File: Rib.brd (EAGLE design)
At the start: 127 x 87.6 mm, 34 parts, among them IC1 REG1117, IC2 REG1117

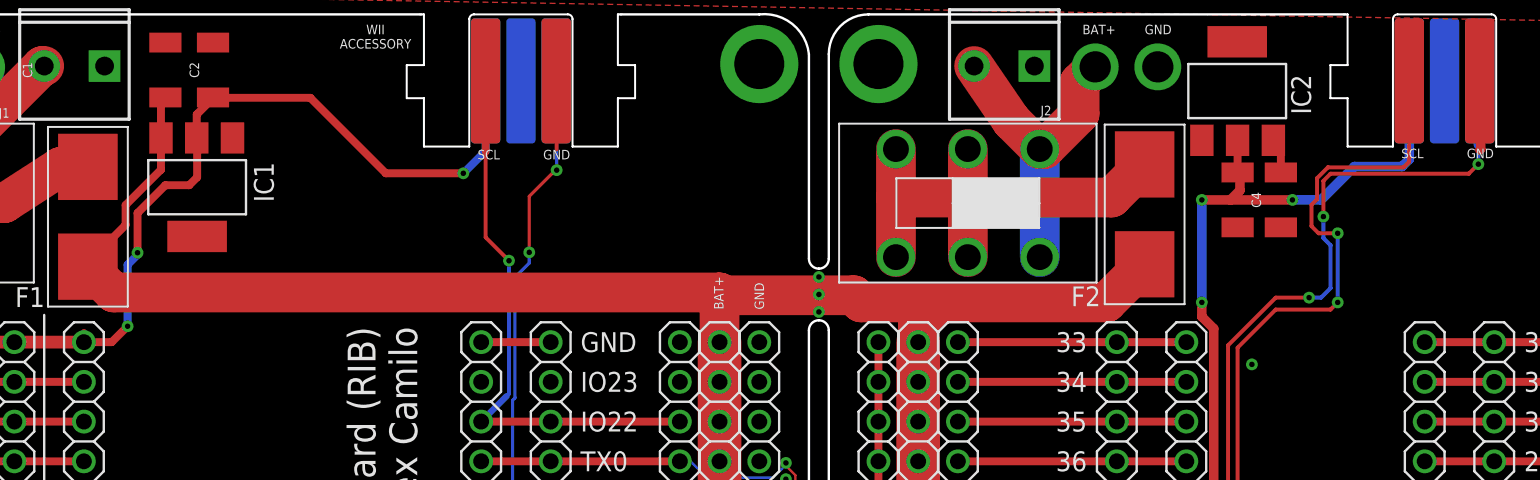
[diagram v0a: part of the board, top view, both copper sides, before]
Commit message: DET pins routed to esp and teensy
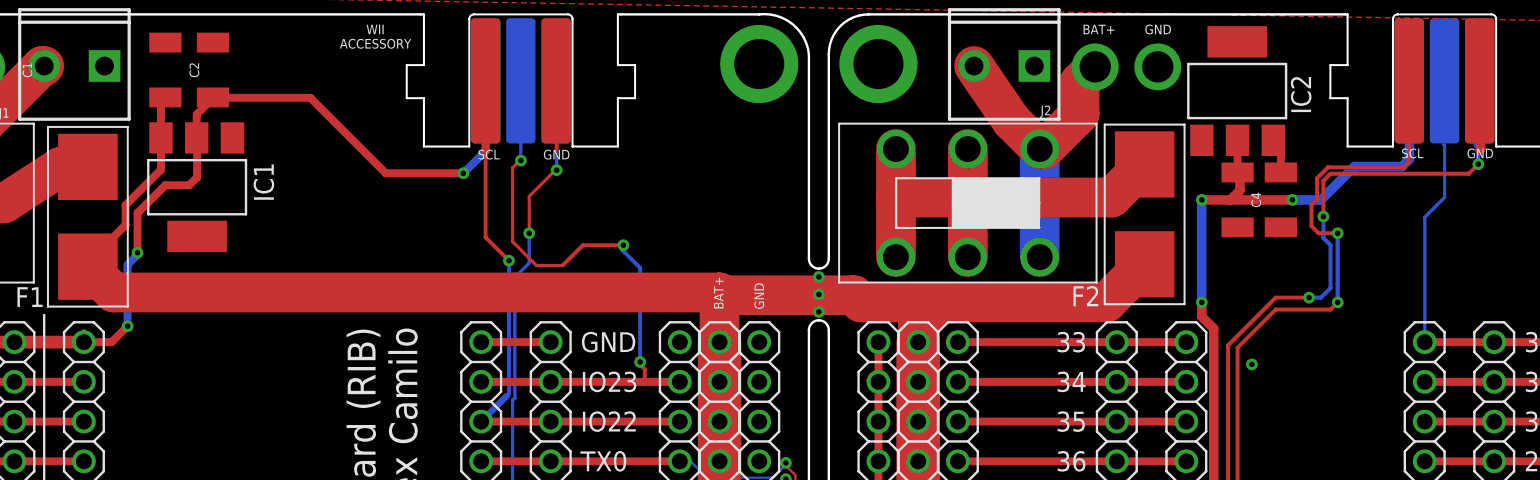
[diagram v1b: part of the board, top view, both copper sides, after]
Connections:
- removed net N$107: JP12.24, JP21.24, JP9.24
- removed net N$24: JP17.18, JP7.18, JP8.18
- new net DET: JP12.24, JP17.18, JP21.24, JP7.18, JP8.18, JP9.24, U$3.ATT, U$5.ATT
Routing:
- net DET: track 0.00 -> 62.5 mm, vias 0 -> 3
- net N$107: track 12.1 -> 0.00 mm
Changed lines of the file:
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@@
 <via x="49.53" y="53.848" extent="1-16" drill="0.35"/>
 <via x="49.53" y="52.7304" extent="1-16" drill="0.35"/>
-<wire x1="4.445" y1="53.975" x2="43.18" y2="53.975" width="2.54" layer="1"/>
+<wire x1="4.445" y1="53.975" x2="30.099" y2="53.975" width="2.54" layer="1"/>
+<wire x1="30.099" y1="53.975" x2="43.18" y2="53.975" width="2.54" layer="1"/>
 <wire x1="67.9196" y1="53.34" x2="70.358" y2="55.7784" width="2.54" layer="1"/>
 <wire x1="67.9196" y1="53.34" x2="57.15" y2="53.34" width="2.54" layer="1"/>
@@
 <via x="29.9466" y="39.243" extent="1-16" drill="0.35"/>
 <wire x1="29.9466" y1="39.243" x2="29.9466" y2="47.08001875" width="0.2032" layer="16"/>
-<wire x1="30.099" y1="54.9402" x2="31.0134" y2="55.8546" width="0.2032" layer="16"/>
 <wire x1="29.9466" y1="47.08001875" x2="30.099" y2="47.23241875" width="0.2032" layer="16"/>
 <wire x1="30.099" y1="47.23241875" x2="30.099" y2="54.9402" width="0.2032" layer="16"/>
-<via x="31.0134" y="56.5404" extent="1-16" drill="0.35"/>
-<wire x1="31.0134" y1="56.5404" x2="31.0134" y2="60.1218" width="0.2032" layer="1"/>
+<via x="31.0134" y="57.7596" extent="1-16" drill="0.35"/>
+<wire x1="31.0134" y1="57.7596" x2="31.0134" y2="60.1218" width="0.2032" layer="1"/>
 <wire x1="31.0134" y1="60.1218" x2="32.6136" y2="61.722" width="0.2032" layer="1"/>
 <wire x1="32.6136" y1="61.722" x2="32.766" y2="61.7982" width="0.2032" layer="1"/>
 <via x="32.766" y="61.7982" extent="1-16" drill="0.35"/>
 <wire x1="32.766" y1="61.7982" x2="32.766" y2="63.627" width="0.2032" layer="16"/>
-<wire x1="31.0134" y1="55.8546" x2="31.0134" y2="56.5404" width="0.2032" layer="16"/>
+<wire x1="30.099" y1="54.9402" x2="31.0134" y2="55.8546" width="0.2032" layer="16"/>
+<wire x1="31.0134" y1="55.8546" x2="31.0134" y2="57.7596" width="0.2032" layer="16"/>
 <wire x1="32.766" y1="63.627" x2="32.639" y2="65.786" width="0" layer="19" extent="16-16"/>
 <wire x1="58.42" y1="12.7" x2="40.64" y2="38.1" width="0" layer="19" extent="1-1"/>
@@
 <wire x1="100.33" y1="48.26" x2="88.265" y2="48.26" width="0.508" layer="1"/>
 <wire x1="88.265" y1="48.26" x2="92.71" y2="48.26" width="0" layer="19" extent="1-1"/>
-</signal>
-<signal name="N$107">
-<contactref element="JP9" pad="24"/>
-<contactref element="JP21" pad="24"/>
-<contactref element="JP12" pad="24"/>
-<wire x1="88.265" y1="50.8" x2="100.33" y2="50.8" width="0.508" layer="1"/>
-<wire x1="88.265" y1="50.8" x2="92.71" y2="50.8" width="0" layer="19" extent="1-1"/>
 </signal>
 <signal name="V3.3">
@@
 <wire x1="26.797" y1="61.595" x2="21.844" y2="61.595" width="0.508" layer="1"/>
 <wire x1="21.844" y1="61.595" x2="17.018" y2="66.421" width="0.508" layer="1"/>
-<wire x1="10.818" y1="66.421" x2="17.018" y2="66.421" width="0.508" layer="1"/>
+<wire x1="17.018" y1="66.421" x2="10.818" y2="66.421" width="0.508" layer="1"/>
 <wire x1="10.818" y1="66.421" x2="10.795" y2="66.444" width="0.508" layer="1"/>
 <wire x1="2.54" y1="50.8" x2="4.318" y2="50.8" width="0.508" layer="1"/>
@@
 <wire x1="66.2" y1="67.4" x2="67.2" y2="68.4" width="2.54" layer="1"/>
 </signal>
-<signal name="N$24">
+<signal name="DET">
 <contactref element="JP17" pad="18"/>
 <contactref element="JP8" pad="18"/>
 <contactref element="JP7" pad="18"/>
-<wire x1="32.385" y1="48.26" x2="40.64" y2="48.26" width="0" layer="19" extent="1-1"/>
-<wire x1="27.94" y1="48.26" x2="32.385" y2="48.26" width="0" layer="19" extent="1-1"/>
+<wire x1="27.94" y1="48.26" x2="32.385" y2="48.26" width="0.508" layer="1"/>
+<wire x1="32.385" y1="48.26" x2="38.4048" y2="48.26" width="0.508" layer="1"/>
+<contactref element="U$3" pad="ATT"/>
+<contactref element="U$5" pad="ATT"/>
+<wire x1="38.4048" y1="48.26" x2="40.64" y2="48.26" width="0.508" layer="1"/>
+<wire x1="38.4048" y1="48.26" x2="38.4048" y2="49.0728" width="0.254" layer="1"/>
+<wire x1="38.4048" y1="49.0728" x2="37.9476" y2="49.53" width="0.254" layer="1"/>
+<wire x1="37.9476" y1="49.53" x2="38.1" y2="49.53" width="0.254" layer="1"/>
+<via x="38.1" y="49.53" extent="1-16" drill="0.35"/>
+<wire x1="38.1" y1="49.53" x2="38.1" y2="55.5498" width="0.254" layer="16"/>
+<wire x1="38.1" y1="55.5498" x2="36.957" y2="56.6928" width="0.254" layer="16"/>
+<wire x1="36.957" y1="56.6928" x2="37.0332" y2="56.769" width="0.254" layer="16"/>
+<wire x1="37.0332" y1="56.769" x2="37.0332" y2="56.9976" width="0.254" layer="16"/>
+<via x="37.0332" y="56.9976" extent="1-16" drill="0.35"/>
+<wire x1="37.0332" y1="56.9976" x2="34.4424" y2="56.9976" width="0.254" layer="1"/>
+<wire x1="34.4424" y1="56.9976" x2="33.147" y2="55.7022" width="0.254" layer="1"/>
+<wire x1="33.147" y1="55.7022" x2="31.4706" y2="55.7022" width="0.2032" layer="1"/>
+<wire x1="31.4706" y1="55.7022" x2="29.9466" y2="57.2262" width="0.2032" layer="1"/>
+<wire x1="29.9466" y1="57.2262" x2="29.9466" y2="61.9506" width="0.2032" layer="1"/>
+<wire x1="29.9466" y1="61.9506" x2="30.4038" y2="62.4078" width="0.2032" layer="1"/>
+<wire x1="30.4038" y1="62.4078" x2="30.48" y2="62.4078" width="0.2032" layer="1"/>
+<via x="30.48" y="62.4078" extent="1-16" drill="0.35"/>
+<wire x1="30.48" y1="62.4078" x2="30.48" y2="63.5508" width="0.2032" layer="16"/>
+<wire x1="30.48" y1="63.5508" x2="30.4038" y2="63.627" width="0.2032" layer="16"/>
+<contactref element="JP9" pad="24"/>
+<contactref element="JP21" pad="24"/>
+<contactref element="JP12" pad="24"/>
+<wire x1="88.265" y1="50.8" x2="100.33" y2="50.8" width="0.508" layer="1"/>
+<wire x1="88.265" y1="50.8" x2="88.265" y2="58.7756" width="0.2032" layer="16"/>
+<wire x1="88.265" y1="58.7756" x2="89.535" y2="60.0456" width="0.2032" layer="16"/>
+<wire x1="89.535" y1="60.0456" x2="89.535" y2="63.373" width="0.2032" layer="16"/>
+<wire x1="89.535" y1="63.373" x2="89.4588" y2="63.4492" width="0.2032" layer="16"/>
+<wire x1="89.4588" y1="63.4492" x2="89.535" y2="67.505" width="0" layer="19" extent="16-16"/>
+<wire x1="92.71" y1="50.8" x2="88.265" y2="50.8" width="0" layer="19" extent="1-1"/>
+<wire x1="40.64" y1="48.26" x2="88.265" y2="50.8" width="0" layer="19" extent="1-1"/>
+<wire x1="30.48" y1="67.505" x2="30.4038" y2="63.627" width="0" layer="19" extent="16-16"/>
 </signal>
 </signals>
